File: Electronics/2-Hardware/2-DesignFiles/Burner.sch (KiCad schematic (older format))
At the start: 60 parts, among them P1 CONN_2, P10 CONN_1, P2 CONN_1, P3 CONN_1, P4 CONN_01X03, P5 CONN_01X04, P6 CONN_1, P7 CONN_4, P8 CONN_1, P9 CONN_1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

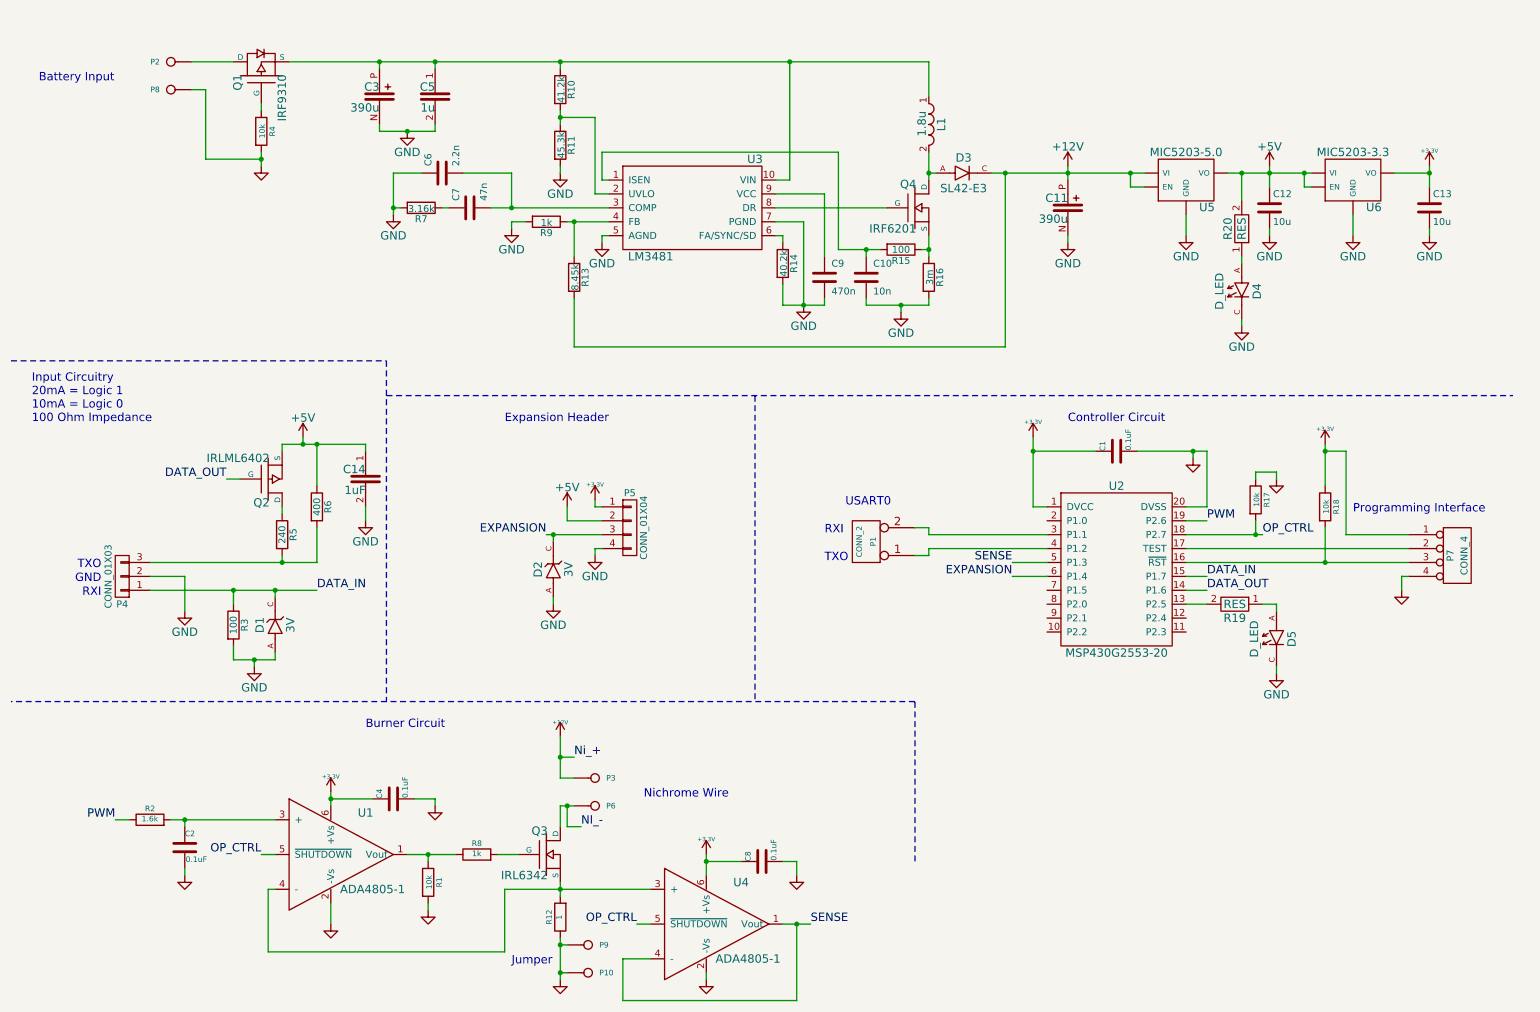
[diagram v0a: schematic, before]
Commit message: Updated component part numbers
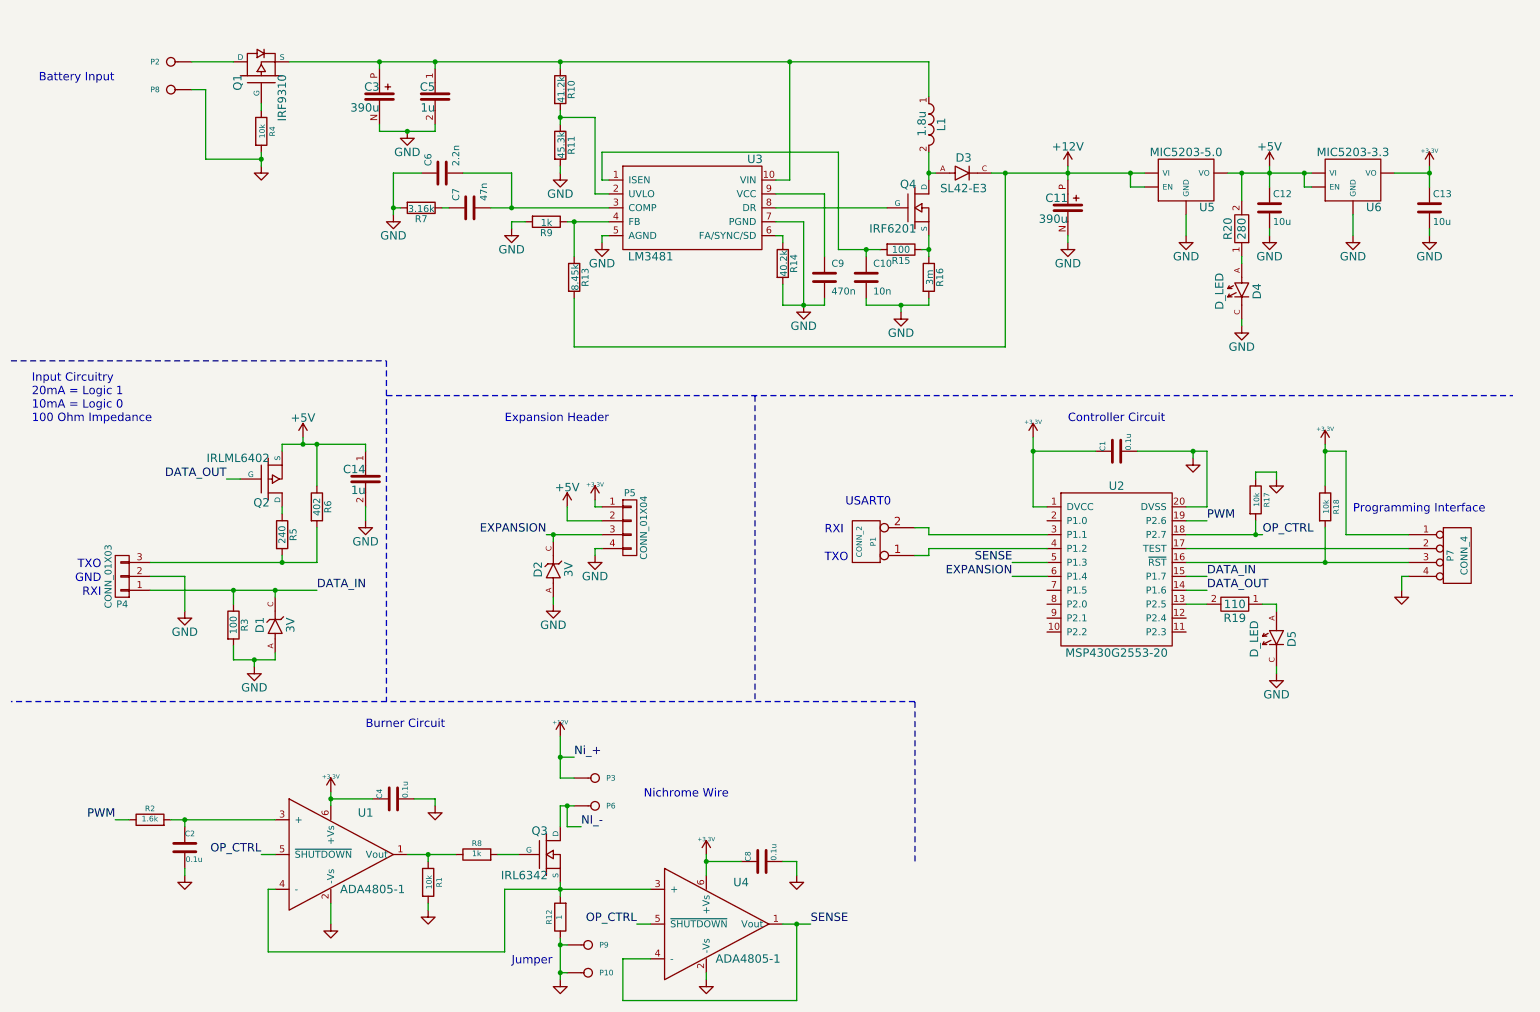
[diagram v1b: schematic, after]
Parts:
- C1: value 0.1uF -> 0.1u; DigikeyNumber (none) -> 311-1141-1-ND; DigikeyPart 311-1141-1-ND -> (none)
- C10: DigikeyNumber (none) -> 311-1136-1-ND; Manufacturer (none) -> Yageo; ManufacturerNumber (none) -> CC0805KRX7R9BB103
- C11: DigikeyNumber (none) -> P16500CT-ND; Manufacturer (none) -> Panasonic Electronics Components; ManufacturerNumber (none) -> 20SVPF390M
- C12, C13: DigikeyNumber (none) -> 311-1355-1-ND; Manufacturer (none) -> Yageo; ManufacturerNumber (none) -> CC0805ZKY5V6BB106
- C14: value 1uF -> 1u; DigikeyNumber (none) -> 311-1365-1-ND; Manufacturer (none) -> Yageo; ManufacturerNumber (none) -> CC0805KKX7R7BB105
- C2, C4, C8: value 0.1uF -> 0.1u; DigikeyNumber (none) -> 311-1141-1-ND; Manufacturer (none) -> Yageo; ManufacturerNumber (none) -> CC0805KRX7R8BB104
- C3: DigikeyNumber (none) -> P16500CT-ND; Manufacturer (none) -> Panasonic Electronic Components; ManufacturerNumber (none) -> 20SVPF390M
- C5: DigikeyNumber (none) -> 311-1365-1-ND; Manufacturer (none) -> Yageo; ManufacturerNumber (none) -> CC0805KKX7R7BB105
- C6: DigikeyNumber (none) -> 311-1129-1-ND; Manufacturer (none) -> Yageo; ManufacturerNumber (none) -> CC0805KRX7R9BB222
- C7: DigikeyNumber (none) -> 311-1431-1-ND; Manufacturer (none) -> Yageo; ManufacturerNumber (none) -> CC0805KRX7R9BB473
- C9: DigikeyNumber (none) -> 311-1364-1-ND; Manufacturer (none) -> Yageo; ManufacturerNumber (none) -> CC0805KKX7R8BB474
- D4, D5: DigikeyNumber (none) -> 754-1141-1-ND; Manufacturer (none) -> Kingbright; ManufacturerNumber (none) -> APT3216SGC
- R1: DigikeyNumber (none) -> P10.0KCCT-ND; DigikeyPart P10.0KCCT-ND -> (none); Manufacturer Panasonic Electronics Components -> Panasonic Electronic Components
- R10: DigikeyNumber (none) -> P41.2KCCT-ND; Manufacturer (none) -> Panasonic Electronic Components; ManufacturerNumber (none) -> ERJ-6ENF4122V
- R11: DigikeyNumber (none) -> P45.3KCCT-ND; Manufacturer (none) -> Panasonic Electronic Components; ManufacturerNumber (none) -> ERJ-6ENF4532V
- R13: DigikeyNumber (none) -> P8.45KCCT-ND; Manufacturer (none) -> Panasonic Electronic Components; ManufacturerNumber (none) -> ERJ-6ENF8451V
- R14: DigikeyNumber (none) -> P40.2KCCT-ND; Manufacturer (none) -> Panasonic Electronic Components; ManufacturerNumber (none) -> ERJ-6ENF4022V
- R15, R3: DigikeyNumber (none) -> P100CCT-ND; Manufacturer (none) -> Panasonic Electronic Components; ManufacturerNumber (none) -> ERJ-6ENF1000V
- R17, R18, R4: DigikeyNumber (none) -> P10.0KCCT-ND; Manufacturer (none) -> Panasonic Electronic Components; ManufacturerNumber (none) -> ERJ-6ENF1002V
- R19: value RES -> 110; DigikeyNumber (none) -> P110CCT-ND; Manufacturer (none) -> Panasonic Electronic Components; ManufacturerNumber (none) -> ERJ-6ENF1100V
- R2: DigikeyNumber (none) -> P1.60KCCT-ND; Manufacturer (none) -> Panasonic Electronic Components; ManufacturerNumber (none) -> ERJ-6ENF1601V
- R20: value RES -> 280; DigikeyNumber (none) -> P280CCT-ND; Manufacturer (none) -> Panasonic Electronic Components; ManufacturerNumber (none) -> ERJ-6ENF2800V
- R5: DigikeyNumber (none) -> P240CCT-ND; Manufacturer (none) -> Panasonic Electronic Components; ManufacturerNumber (none) -> ERJ-6ENF2400V
- R6: value 400 -> 402; DigikeyNumber (none) -> P402CCT-ND; Manufacturer (none) -> Panasonic Electronic Components; ManufacturerNumber (none) -> ERJ-6ENF4020V
- R7: DigikeyNumber (none) -> P3.16KCCT-ND; Manufacturer (none) -> Panasonic Electronic Components; ManufacturerNumber (none) -> ERJ-6ENF3161V
- R8: DigikeyNumber (none) -> P1.00KCCT-ND; Manufacturer (none) -> Panasonic Electronic Components; ManufacturerNumber (none) -> ERJ-6ENF1001V
- R9: DigikeyNumber (none) -> P1.00KCCT-ND; Manufacturer (none) -> Panasonic Electronics Components; ManufacturerNumber (none) -> ERJ-6ENF1001V
- U2: DigikeyNumber (none) -> 296-28430-1-ND; DigikeyPart 296-28430-1-ND -> (none)
- U5: DigikeyNumber (none) -> 576-2734-1-ND; DigikeyPart 576-2734-1-ND -> (none)

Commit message: Changed transconductance op-amp power supply. Reorganized schematic
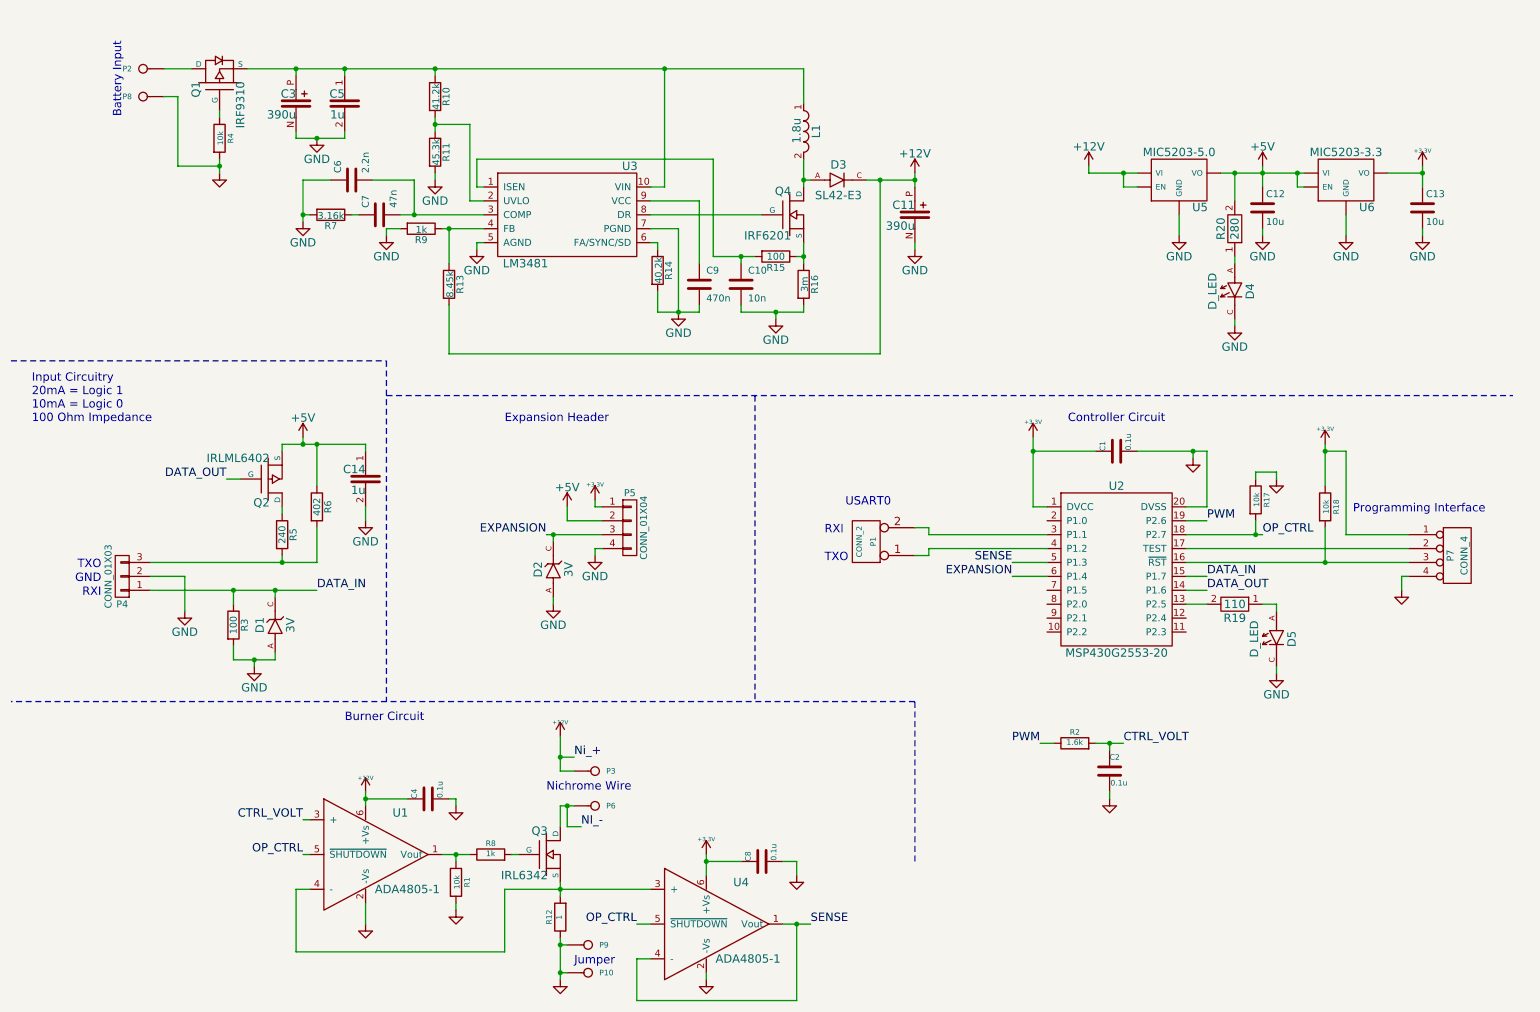
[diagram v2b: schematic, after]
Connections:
- net +12V: now also C4.1, U1.6 (+Vs)
- net +3V3: no longer C4.1, U1.6 (+Vs)
- net CTRL_VOLT: now reaches C2.1, R2.2, U1.3 (+)
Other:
- moved on the sheet: C10, C11, C12, C13, C2, C3, C4, C5, C6, C7, C9, D3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
